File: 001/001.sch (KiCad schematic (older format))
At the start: 7 parts, among them J1 USB_C_Receptacle_USB2.0, J2 Conn_01x14

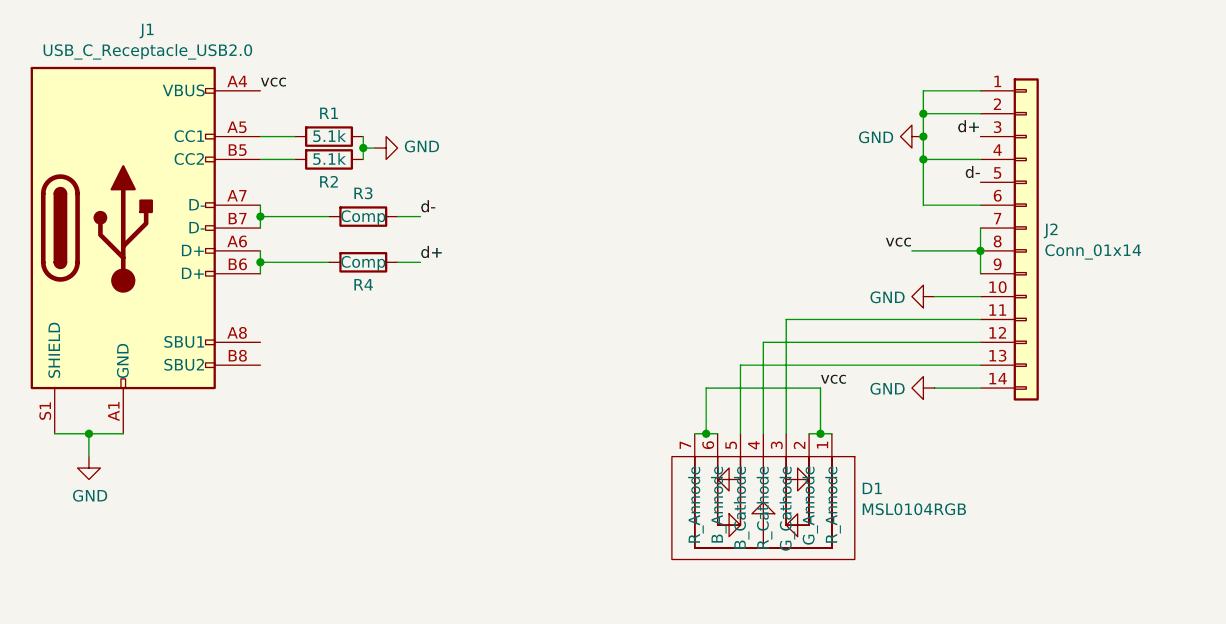
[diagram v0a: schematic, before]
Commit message: Updated schematic, added addtiional info and images to readme
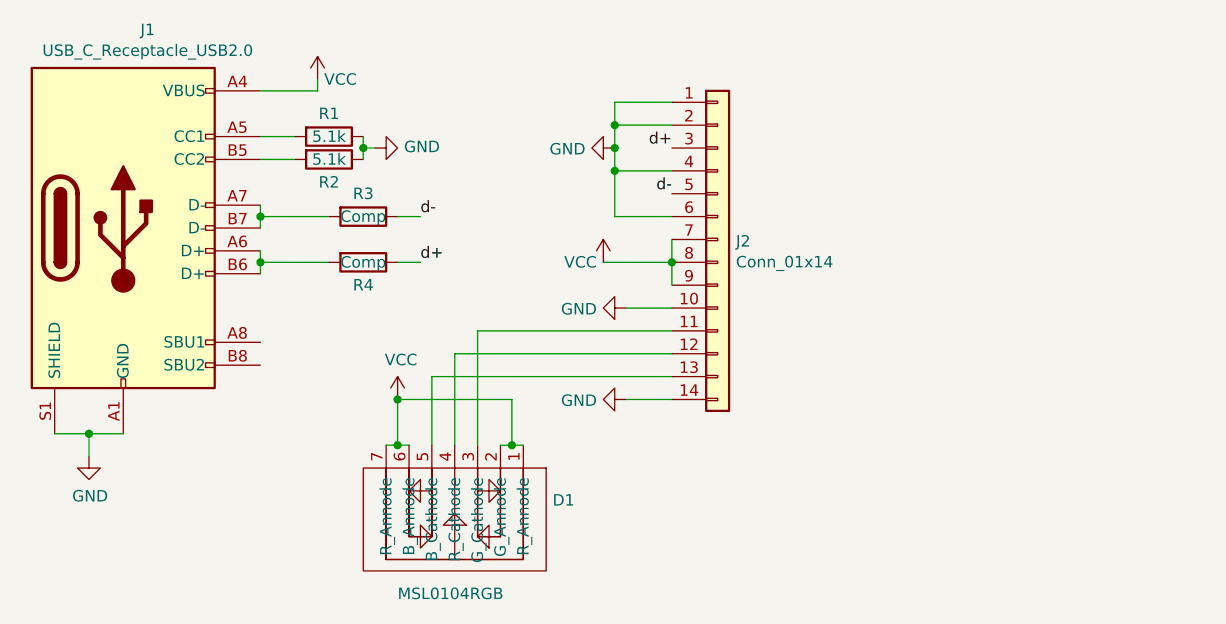
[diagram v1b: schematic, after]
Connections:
- net vcc renamed VCC
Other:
- moved on the sheet: D1, J2
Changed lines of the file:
@@
 EELAYER 30 0
 EELAYER END
-$Descr A4 11693 8268
+$Descr User 7283 5157
 encoding utf-8
 Sheet 1 1
@@
 L Connector_Generic:Conn_01x14 J2
 U 1 1 611858EF
-P 5050 1550
-F 0 "J2" H 5130 1542 50  0000 L CNN
-F 1 "Conn_01x14" H 5130 1451 50  0000 L CNN
-F 2 "Molex 503480-1400:503480-1400" H 5050 1550 50  0001 C CNN
-F 3 "~" H 5050 1550 50  0001 C CNN
-	1    5050 1550
+P 3700 1600
+F 0 "J2" H 3780 1592 50  0000 L CNN
+F 1 "Conn_01x14" H 3780 1501 50  0000 L CNN
+F 2 "Molex 503480-1400:503480-1400" H 3700 1600 50  0001 C CNN
+F 3 "~" H 3700 1600 50  0001 C CNN
+	1    3700 1600
 	1    0    0    -1
 $EndComp
@@
 	0    1    1    0
 $EndComp
-Text Label 1700 950  0    50   ~ 0
-vcc
 Text Label 2400 1500 0    50   ~ 0
 d-
@@
 	950  2450 800  2450
 Wire Wire Line
-	4850 1050 4600 1050
-Wire Wire Line
-	4600 1050 4600 1150
-Wire Wire Line
-	4600 1250 4850 1250
+	3500 1100 3250 1100
+Wire Wire Line
+	3250 1100 3250 1200
+Wire Wire Line
+	3250 1300 3500 1300
 $Comp
 L power:GND #PWR03
 U 1 1 6118CE0B
-P 4600 1150
-F 0 "#PWR03" H 4600 900 50  0001 C CNN
-F 1 "GND" V 4605 1022 50  0000 R CNN
-F 2 "" H 4600 1150 50  0001 C CNN
-F 3 "" H 4600 1150 50  0001 C CNN
-	1    4600 1150
-	0    1    1    0
-$EndComp
-Connection ~ 4600 1150
-Wire Wire Line
-	4600 1150 4600 1250
-Wire Wire Line
-	4850 950  4600 950
-Wire Wire Line
-	4600 950  4600 1050
-Connection ~ 4600 1050
-Wire Wire Line
-	4850 1450 4600 1450
-Wire Wire Line
-	4600 1450 4600 1250
-Connection ~ 4600 1250
-Wire Wire Line
-	4850 1550 4850 1650
-Connection ~ 4850 1650
-Wire Wire Line
-	4850 1650 4850 1750
-Wire Wire Line
-	4850 1650 4550 1650
-Text Label 4850 1150 2    50   ~ 0
+P 3250 1200
+F 0 "#PWR03" H 3250 950 50  0001 C CNN
+F 1 "GND" V 3255 1072 50  0000 R CNN
+F 2 "" H 3250 1200 50  0001 C CNN
+F 3 "" H 3250 1200 50  0001 C CNN
+	1    3250 1200
+	0    1    1    0
+$EndComp
+Connection ~ 3250 1200
+Wire Wire Line
+	3250 1200 3250 1300
+Wire Wire Line
+	3500 1000 3250 1000
+Wire Wire Line
+	3250 1000 3250 1100
+Connection ~ 3250 1100
+Wire Wire Line
+	3500 1500 3250 1500
+Wire Wire Line
+	3250 1500 3250 1300
+Connection ~ 3250 1300
+Wire Wire Line
+	3500 1600 3500 1700
+Connection ~ 3500 1700
+Wire Wire Line
+	3500 1700 3500 1800
+Wire Wire Line
+	3500 1700 3200 1700
+Text Label 3500 1200 2    50   ~ 0
 d+
-Text Label 4850 1350 2    50   ~ 0
+Text Label 3500 1400 2    50   ~ 0
 d-
-Text Label 4550 1650 2    50   ~ 0
-vcc
 $Comp
 L power:GND #PWR04
 U 1 1 6118F285
-P 4650 1850
-F 0 "#PWR04" H 4650 1600 50  0001 C CNN
-F 1 "GND" V 4655 1722 50  0000 R CNN
-F 2 "" H 4650 1850 50  0001 C CNN
-F 3 "" H 4650 1850 50  0001 C CNN
-	1    4650 1850
+P 3300 1900
+F 0 "#PWR04" H 3300 1650 50  0001 C CNN
+F 1 "GND" V 3305 1772 50  0000 R CNN
+F 2 "" H 3300 1900 50  0001 C CNN
+F 3 "" H 3300 1900 50  0001 C CNN
+	1    3300 1900
 	0    1    1    0
 $EndComp
@@
 L power:GND #PWR05
 U 1 1 6118F8B2
-P 4650 2250
-F 0 "#PWR05" H 4650 2000 50  0001 C CNN
-F 1 "GND" V 4655 2122 50  0000 R CNN
-F 2 "" H 4650 2250 50  0001 C CNN
-F 3 "" H 4650 2250 50  0001 C CNN
-	1    4650 2250
-	0    1    1    0
-$EndComp
-Wire Wire Line
-	4850 1850 4650 1850
-Wire Wire Line
-	4850 2250 4650 2250
+P 3300 2300
+F 0 "#PWR05" H 3300 2050 50  0001 C CNN
+F 1 "GND" V 3305 2172 50  0000 R CNN
+F 2 "" H 3300 2300 50  0001 C CNN
+F 3 "" H 3300 2300 50  0001 C CNN
+	1    3300 2300
+	0    1    1    0
+$EndComp
+Wire Wire Line
+	3500 1900 3300 1900
+Wire Wire Line
+	3500 2300 3300 2300
 $Comp
 L MSL0104RGB:MSL0104RGB D1
 U 1 1 6119707E
-P 3900 2600
-F 0 "D1" H 3472 2691 50  0000 R CNN
-F 1 "MSL0104RGB" H 3472 2782 50  0000 R CNN
-F 2 "MSL0104RGB:MSL0104RGB" H 3900 2600 50  0001 C CNN
-F 3 "" H 3900 2600 50  0001 C CNN
-	1    3900 2600
+P 2550 2650
+F 0 "D1" H 2122 2741 50  0000 R CNN
+F 1 "MSL0104RGB" H 2800 3150 50  0000 R CNN
+F 2 "MSL0104RGB:MSL0104RGB" H 2550 2650 50  0001 C CNN
+F 3 "" H 2550 2650 50  0001 C CNN
+	1    2550 2650
 	-1   0    0    1
 $EndComp
 Wire Wire Line
-	4200 2450 4150 2450
-Wire Wire Line
-	3600 2450 3650 2450
-Wire Wire Line
-	4150 2450 4150 2250
-Wire Wire Line
-	4150 2250 3650 2250
-Wire Wire Line
-	3650 2250 3650 2450
-Connection ~ 4150 2450
-Wire Wire Line
-	4150 2450 4100 2450
-Connection ~ 3650 2450
-Wire Wire Line
-	3650 2450 3700 2450
-Text Label 4150 2250 0    50   ~ 0
-vcc
-Wire Wire Line
-	3800 2450 3800 2150
-Wire Wire Line
-	3900 2450 3900 2050
-Wire Wire Line
-	4000 2450 4000 1950
-Wire Wire Line
-	3800 2150 4850 2150
-Wire Wire Line
-	3900 2050 4850 2050
-Wire Wire Line
-	4000 1950 4850 1950
+	2850 2500 2800 2500
+Wire Wire Line
+	2250 2500 2300 2500
+Wire Wire Line
+	2800 2500 2800 2300
+Wire Wire Line
+	2800 2300 2300 2300
+Wire Wire Line
+	2300 2300 2300 2500
+Connection ~ 2800 2500
+Wire Wire Line
+	2800 2500 2750 2500
+Connection ~ 2300 2500
+Wire Wire Line
+	2300 2500 2350 2500
+Wire Wire Line
+	2450 2500 2450 2200
+Wire Wire Line
+	2550 2500 2550 2100
+Wire Wire Line
+	2650 2500 2650 2000
+Wire Wire Line
+	2450 2200 3500 2200
+Wire Wire Line
+	2550 2100 3500 2100
+Wire Wire Line
+	2650 2000 3500 2000
+$Comp
+L power:VCC #PWR?
+U 1 1 621ACE38
+P 3200 1700
+F 0 "#PWR?" H 3200 1550 50  0001 C CNN
+F 1 "VCC" H 3100 1700 50  0000 C CNN
+F 2 "" H 3200 1700 50  0001 C CNN
+F 3 "" H 3200 1700 50  0001 C CNN
+	1    3200 1700
+	1    0    0    -1
+$EndComp
+$Comp
+L power:VCC #PWR?
+U 1 1 621AD55C
+P 2300 2300
+F 0 "#PWR?" H 2300 2150 50  0001 C CNN
+F 1 "VCC" H 2315 2473 50  0000 C CNN
+F 2 "" H 2300 2300 50  0001 C CNN
+F 3 "" H 2300 2300 50  0001 C CNN
+	1    2300 2300
+	1    0    0    -1
+$EndComp
+Connection ~ 2300 2300
+$Comp
+L power:VCC #PWR?
+U 1 1 621AC206
+P 1950 900
+F 0 "#PWR?" H 1950 750 50  0001 C CNN
+F 1 "VCC" H 2050 900 50  0000 C CNN
+F 2 "" H 1950 900 50  0001 C CNN
+F 3 "" H 1950 900 50  0001 C CNN
+	1    1950 900
+	1    0    0    -1
+$EndComp
+Wire Wire Line
+	1700 950  1950 950
+Wire Wire Line
+	1950 950  1950 900
 $EndSCHEMATC

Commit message: Modified 001 to have pads to be used for 011 as well.
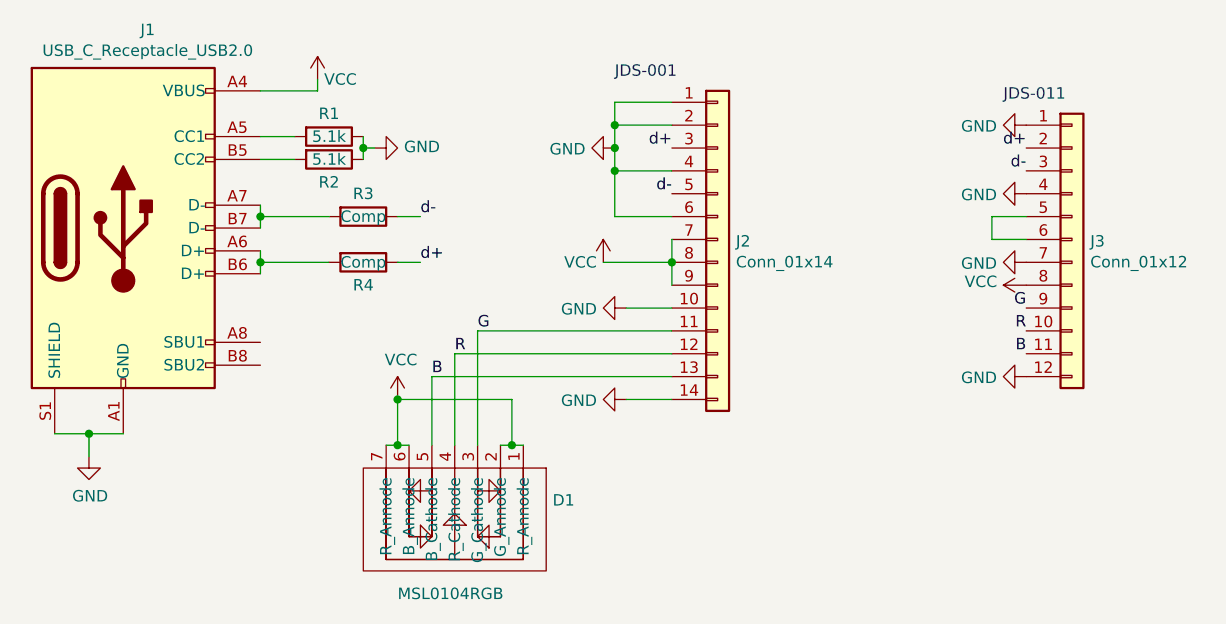
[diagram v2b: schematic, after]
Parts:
- added J3: Conn_01x12, Molex 5034801200:503480-1200, symbol Connector_Generic:Conn_01x12
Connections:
- net GND: now also J3.1 (Pin_1), J3.12 (Pin_12), J3.4 (Pin_4), J3.7 (Pin_7)
- net VCC: now also J3.8 (Pin_8)
- net d+: now also J3.2 (Pin_2)
- net d-: now also J3.3 (Pin_3)
- net G: now reaches D1.3 (G_Cathode), J2.11 (Pin_11)
- net G: now also J3.9 (Pin_9)
- net R: now reaches D1.4 (R_Cathode), J2.12 (Pin_12)
- net R: now also J3.10 (Pin_10)
- net B: now reaches D1.5 (B_Cathode), J2.13 (Pin_13)
- net B: now also J3.11 (Pin_11)
- new net: J3.5 (Pin_5), J3.6 (Pin_6)
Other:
- note added: "JDS-001"
- note added: "JDS-011"
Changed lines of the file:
@@
 	2650 2000 3500 2000
 $Comp
-L power:VCC #PWR?
+L power:VCC #PWR08
 U 1 1 621ACE38
 P 3200 1700
-F 0 "#PWR?" H 3200 1550 50  0001 C CNN
+F 0 "#PWR08" H 3200 1550 50  0001 C CNN
 F 1 "VCC" H 3100 1700 50  0000 C CNN
 F 2 "" H 3200 1700 50  0001 C CNN
@@
 $EndComp
 $Comp
-L power:VCC #PWR?
+L power:VCC #PWR07
 U 1 1 621AD55C
 P 2300 2300
-F 0 "#PWR?" H 2300 2150 50  0001 C CNN
+F 0 "#PWR07" H 2300 2150 50  0001 C CNN
 F 1 "VCC" H 2315 2473 50  0000 C CNN
 F 2 "" H 2300 2300 50  0001 C CNN
@@
 Connection ~ 2300 2300
 $Comp
-L power:VCC #PWR?
+L power:VCC #PWR06
 U 1 1 621AC206
 P 1950 900
-F 0 "#PWR?" H 1950 750 50  0001 C CNN
+F 0 "#PWR06" H 1950 750 50  0001 C CNN
 F 1 "VCC" H 2050 900 50  0000 C CNN
 F 2 "" H 1950 900 50  0001 C CNN
@@
 Wire Wire Line
 	1950 950  1950 900
+$Comp
+L Connector_Generic:Conn_01x12 J3
+U 1 1 622288ED
+P 5250 1600
+F 0 "J3" H 5330 1592 50  0000 L CNN
+F 1 "Conn_01x12" H 5330 1501 50  0000 L CNN
+F 2 "Molex 5034801200:503480-1200" H 5250 1600 50  0001 C CNN
+F 3 "~" H 5250 1600 50  0001 C CNN
+	1    5250 1600
+	1    0    0    -1
+$EndComp
+Text Notes 3250 900  0    50   ~ 0
+JDS-001
+Text Notes 4950 1000 0    50   ~ 0
+JDS-011
+$Comp
+L power:GND #PWR09
+U 1 1 6222AF9C
+P 5050 1100
+F 0 "#PWR09" H 5050 850 50  0001 C CNN
+F 1 "GND" V 5055 972 50  0000 R CNN
+F 2 "" H 5050 1100 50  0001 C CNN
+F 3 "" H 5050 1100 50  0001 C CNN
+	1    5050 1100
+	0    1    1    0
+$EndComp
+Text Label 5050 1200 2    50   ~ 0
+d+
+Text Label 5050 1300 2    50   ~ 0
+d-
+$Comp
+L power:GND #PWR010
+U 1 1 6222BE64
+P 5050 1400
+F 0 "#PWR010" H 5050 1150 50  0001 C CNN
+F 1 "GND" V 5055 1272 50  0000 R CNN
+F 2 "" H 5050 1400 50  0001 C CNN
+F 3 "" H 5050 1400 50  0001 C CNN
+	1    5050 1400
+	0    1    1    0
+$EndComp
+Wire Wire Line
+	5050 1500 4900 1500
+Wire Wire Line
+	4900 1500 4900 1600
+Wire Wire Line
+	4900 1600 5050 1600
+$Comp
+L power:GND #PWR011
+U 1 1 6222D072
+P 5050 1700
+F 0 "#PWR011" H 5050 1450 50  0001 C CNN
+F 1 "GND" V 5055 1572 50  0000 R CNN
+F 2 "" H 5050 1700 50  0001 C CNN
+F 3 "" H 5050 1700 50  0001 C CNN
+	1    5050 1700
+	0    1    1    0
+$EndComp
+$Comp
+L power:VCC #PWR012
+U 1 1 6222D542
+P 5050 1800
+F 0 "#PWR012" H 5050 1650 50  0001 C CNN
+F 1 "VCC" V 5065 1927 50  0000 L CNN
+F 2 "" H 5050 1800 50  0001 C CNN
+F 3 "" H 5050 1800 50  0001 C CNN
+	1    5050 1800
+	0    -1   -1   0
+$EndComp
+Text Label 5050 1900 2    50   ~ 0
+G
+Text Label 5050 2000 2    50   ~ 0
+R
+Text Label 5050 2100 2    50   ~ 0
+B
+$Comp
+L power:GND #PWR013
+U 1 1 6222EAD6
+P 5050 2200
+F 0 "#PWR013" H 5050 1950 50  0001 C CNN
+F 1 "GND" V 5055 2072 50  0000 R CNN
+F 2 "" H 5050 2200 50  0001 C CNN
+F 3 "" H 5050 2200 50  0001 C CNN
+	1    5050 2200
+	0    1    1    0
+$EndComp
+Text Label 2650 2000 0    50   ~ 0
+G
+Text Label 2550 2100 0    50   ~ 0
+R
+Text Label 2450 2200 0    50   ~ 0
+B
 $EndSCHEMATC
